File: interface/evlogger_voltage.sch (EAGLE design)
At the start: 10 parts, among them IC1 LMV358SOIC

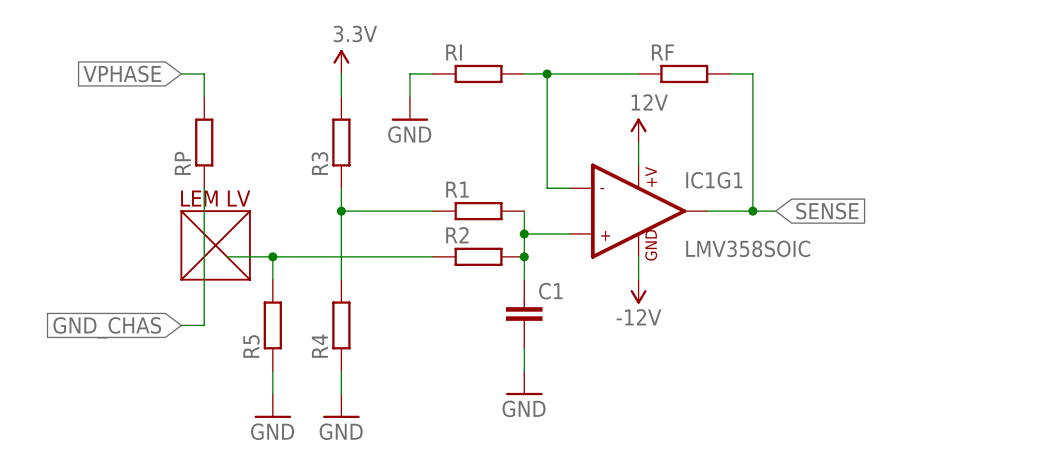
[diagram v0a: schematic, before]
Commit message: Added transient voltage suppression diodes to op amp output
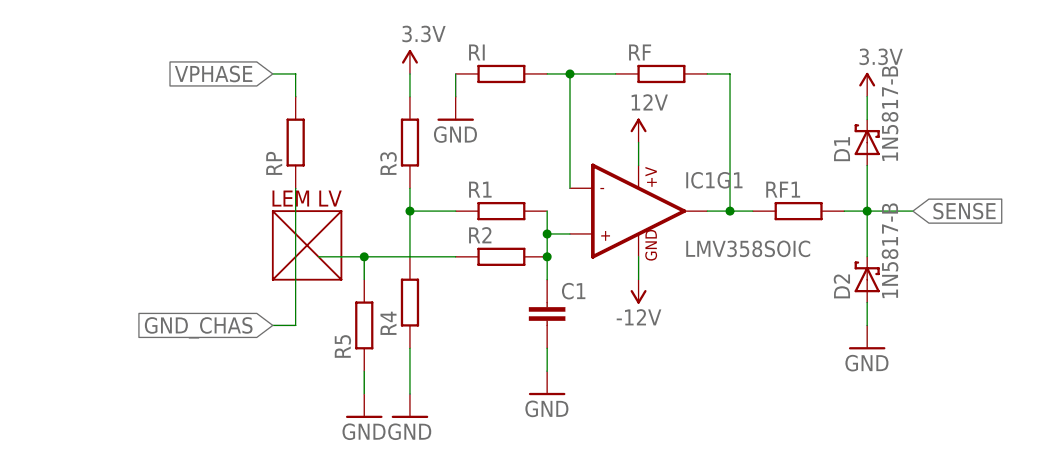
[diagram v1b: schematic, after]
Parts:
- added D1, D2: 1N5817-B, diode:1N5817-B
- added RF1: (no value), rcl:R-EU_0207/10
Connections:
- new net SENS: IC1G1.OUT1, RF.2, RF1.1
- net 3.3V: now also D1.C
- net GND: now also D2.A
- net SENSE: now also D1.A, D2.C, RF1.2; no longer IC1G1.OUT1, RF.2
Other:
- moved on the sheet: C1, R1, R2, R3, R4, R5, RF, RI, RP
